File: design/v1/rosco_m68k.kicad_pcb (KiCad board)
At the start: 4 copper layers, 160 x 100 mm, 78 parts, among them IC1 MC68030RC_PGA, IC15 555N, IC4 XR68C681CJTR-F, J1 UART_A, J2 UART_B, J3 Conn_02x32_Odd_Even, J4 Conn_01x06, J5 PWR, J6 Conn_01x05_Male, J7 Conn_01x01_Male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

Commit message: Initial pin fit
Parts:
- U5: value ATF1504 -> ATF1508
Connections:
- U5 pad 10: A22 -> A23
- U5 pad 11: A8 -> A22
- U5 pad 12: A10 -> A8
- U5 pad 15: A15 -> A10
- U5 pad 16: A13 -> A15
- U5 pad 17: A18 -> A13
- U5 pad 18: A7 -> A18
- U5 pad 20: A11 -> A7
- U5 pad 21: A9 -> A11
- U5 pad 22: A6 -> A9
- U5 pad 24: A3 -> A6
- U5 pad 25: A2 -> A3
- U5 pad 27: A1 -> A2
- U5 pad 28: A0 -> A1
- U5 pad 29: IRQ2 -> A0
- U5 pad 3: A19 -> VCC
- U5 pad 30: IRQ3 -> IRQ2
- U5 pad 31: IRQ5 -> IRQ3
- U5 pad 33: IRQ6 -> IRQ5
- U5 pad 34: SIZ0 -> IRQ6
- U5 pad 35: LDS -> SIZ0
- U5 pad 36: SIZ1 -> LDS
- U5 pad 37: UDS -> SIZ1
- U5 pad 39: RW -> UDS
- U5 pad 4: A14 -> A19
- U5 pad 40: unconnected-(U5-I/O-Pad40) -> RW
- U5 pad 44: unconnected-(U5-I/O-Pad44) -> ODDROMSEL
- U5 pad 45: EVENRAMSEL -> ODDRAMSEL
- U5 pad 46: ODDRAMSEL -> EVENROMSEL
- U5 pad 48: EVENROMSEL -> EVENRAMSEL
- U5 pad 49: ODDROMSEL -> unconnected-(U5-I/O-Pad49)
- U5 pad 5: A21 -> A14
- U5 pad 54: DTACK -> DUASEL
- U5 pad 56: DUASEL -> DTACK
- U5 pad 6: A16 -> A21
- U5 pad 8: A20 -> A16
- U5 pad 9: A23 -> A20
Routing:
- net A0: track 63.6 -> 131.9 mm, vias 3 -> 1
- net RW: track 232.4 -> 293.9 mm
- net A23: track 143.2 -> 195.5 mm, vias 0 -> 2
- net RESET: track 284.6 -> 244.8 mm, vias 3 -> 0
- net E: track 182.2 -> 143.3 mm, vias 1 -> 2
- net D8: track 205.2 -> 167.2 mm
- net IOSEL: track 174.7 -> 138.4 mm, vias 1 -> 2
- net A8: track 254.9 -> 218.6 mm, vias 4 -> 1
- net D9: track 206.3 -> 172.3 mm, vias 6 -> 1
- net A21: track 148.8 -> 178.2 mm, vias 1 -> 3
- net UD9: track 14.5 -> 43.0 mm
- net BERR: track 186.1 -> 157.7 mm, vias 1 -> 2
- net D6: track 210.0 -> 182.8 mm, vias 2 -> 1
- net D10: track 182.6 -> 156.6 mm
- net A15: track 212.9 -> 188.1 mm, vias 1 -> 4
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
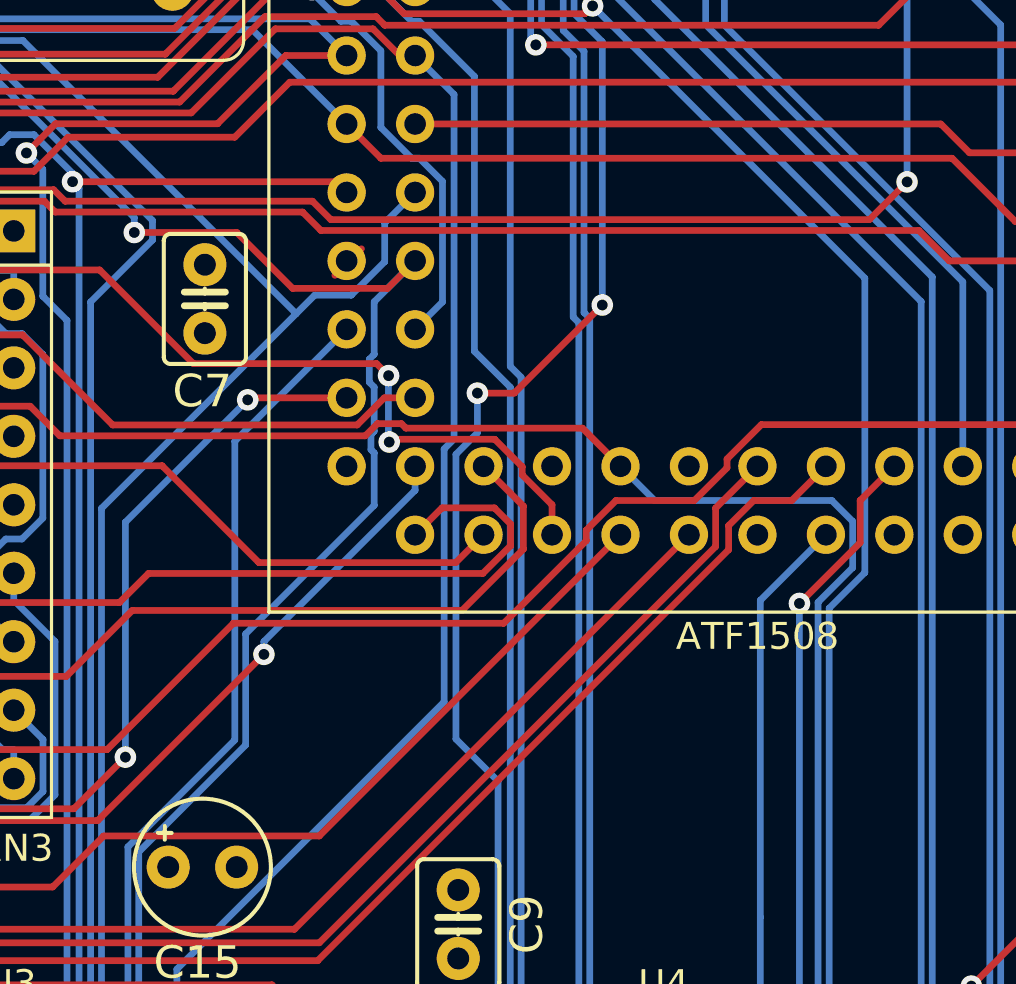
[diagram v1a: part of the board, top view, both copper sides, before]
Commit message: Move ATF1508 VCCIO Cap and correct IRQ code
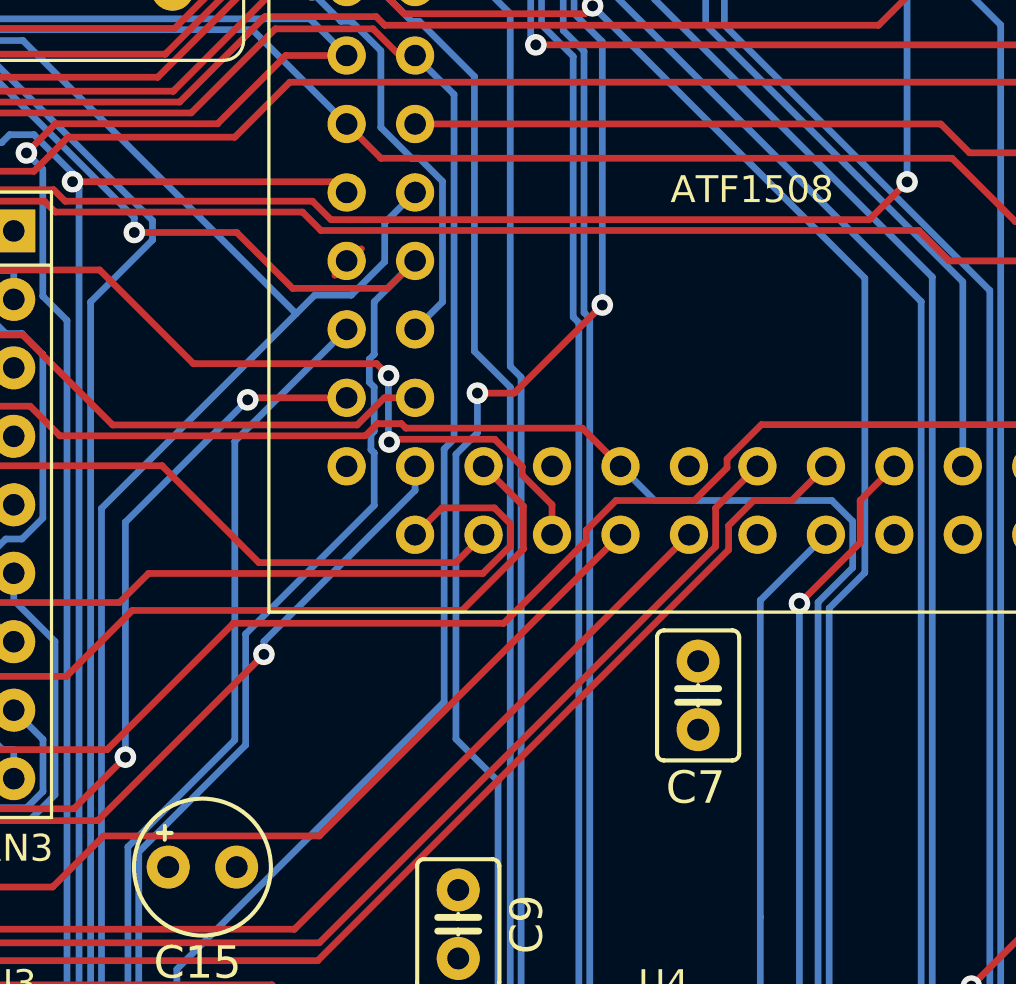
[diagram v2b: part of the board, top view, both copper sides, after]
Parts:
- moved C7 23.5 mm to (168.7, 98.8)
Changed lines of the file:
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@@
 		)
 		(property "Value" "ATF1508"
-			(at 0 34.25 0)
+			(at -0.2 17.6754 0)
 			(layer "F.SilkS")
 			(effects
@@
 	(footprint "rosco_m68k:C2.5-3"
 		(layer "F.Cu")
-		(at 150.4 84.09 -90)
+		(at 168.7 98.8 -90)
 		(descr "<B>MKS2</B>, 5 x 3 mm, grid 2.54 mm")
 		(property "Reference" "C7"

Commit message: Tidy up readme
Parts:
- removed C11: 100uF, rosco_m68k:E2,5-5
- removed C13: 100nF, rosco_m68k:C2.5-3
- removed IC15: 555N, Package_DIP:DIP-8_W7.62mm_LongPads
- removed LED3: GREEN, rosco_m68k:LED5MM
- removed LED4: RED, rosco_m68k:LED5MM
- removed R13, R14: 330R, rosco_m68k:0207_10
- removed R27: 2K2, rosco_m68k:0207_10
- removed R28: 270R, rosco_m68k:0207_10
- removed R31, R32: 4K7, rosco_m68k:0207_10
- removed S1: 10-XX, rosco_m68k:B3F-10XX
- added C37: 0.01uF, rosco_m68k:C2.5-3, F.Cu at (209.5, 72.7)
- added IC9: DS1233-10+, Package_TO_SOT_THT:TO-92, F.Cu at (210.0, 69.3)
- added LED5: RED, rosco_m68k:LED5MM, F.Cu at (216.9, 60.8)
- added LED6: GREEN, rosco_m68k:LED5MM, F.Cu at (210.3, 60.9)
- added R5: 1K, rosco_m68k:0207_10, F.Cu at (216.8, 70.6)
- added R6: 1K, rosco_m68k:0207_10, F.Cu at (213.9, 70.6)
- added SW1: SW_Push, rosco_m68k:B3F-10XX, F.Cu at (221.9, 70.6)
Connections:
- IC1 pad F12: RESET -> HALT
- IC4 pad 38: RESET -> HALT
- J3 pad 36: RESET -> HALT
- U5 pad 1: RESET -> HALT
- U5 pad 67: HALT -> unconnected-(U5-I/O-Pad67)
- U5 pad 68: RESET -> unconnected-(U5-I/O-Pad68)
- U5 pad 69: RUNLED -> unconnected-(U5-I/O-Pad69)
- U5 pad 76: HWRST -> unconnected-(U5-I/O-Pad76)
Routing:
- net RESET: track 244.8 -> 0.00 mm
- net HALT: track 91.5 -> 252.3 mm
- net A12: track 273.4 -> 357.6 mm
- net RW: track 293.9 -> 237.9 mm
- net MMUDIS: track 66.3 -> 117.9 mm, vias 0 -> 1
- net BR: track 89.1 -> 127.0 mm
- net HWRST: track 37.7 -> 0.00 mm
- net A0: track 131.9 -> 96.0 mm, vias 1 -> 2
- net Net-(IC15-THR): track 32.8 -> 0.00 mm
- net A15: track 188.1 -> 220.6 mm, vias 4 -> 3
- net AS: track 145.7 -> 178.1 mm, vias 3 -> 2
- net A20: track 157.9 -> 189.5 mm, vias 4 -> 3
- net RUNLED: track 30.3 -> 0.00 mm
- net A9: track 262.1 -> 232.9 mm, vias 4 -> 3
- net A22: track 163.8 -> 135.1 mm
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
